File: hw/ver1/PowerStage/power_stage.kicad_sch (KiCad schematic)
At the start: 83 parts, among them J7 Conn_01x02_Socket, Q3 BSS138, Q4 BSS138, Q5 BSS84, Q6 BSS138, SW1 SW_DIP_x03, U2 74HC4051PW, U3 LTC7871, U4 LM1117MP-3.3

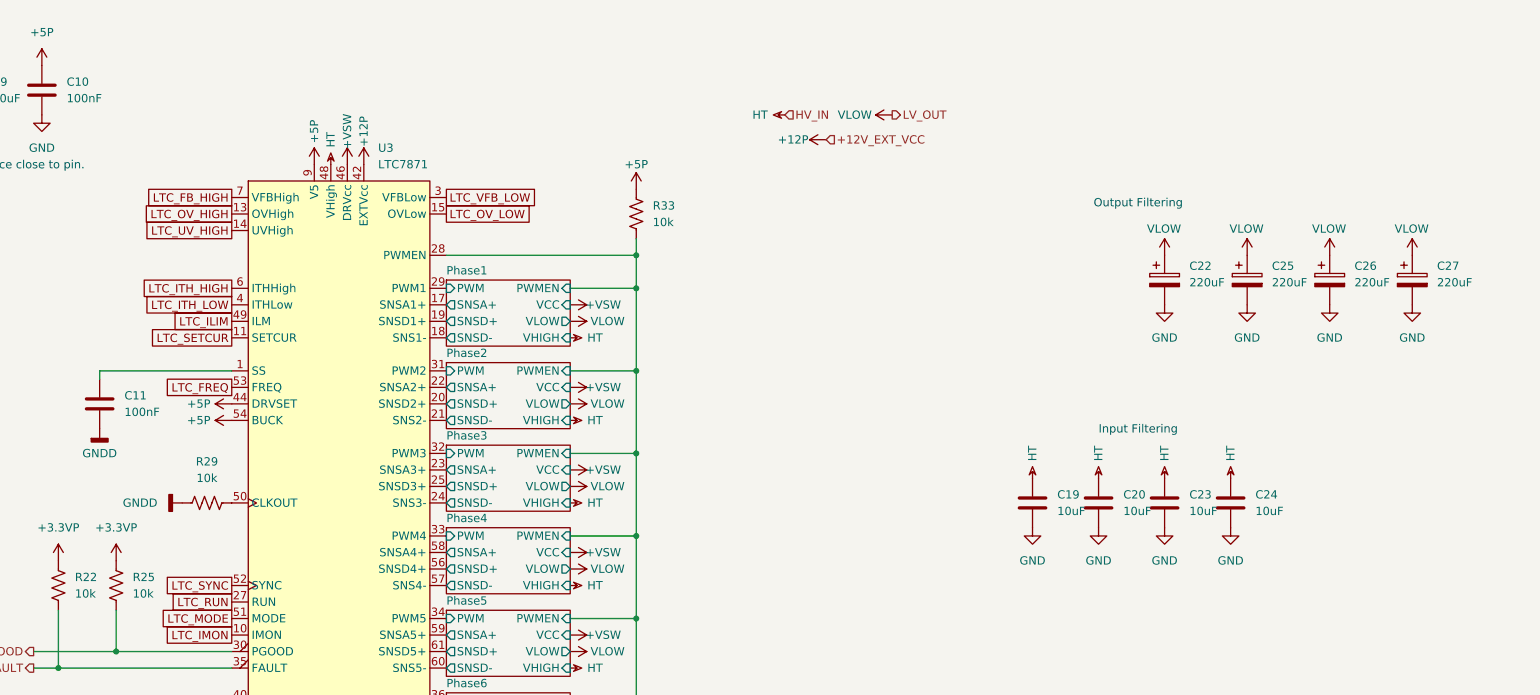
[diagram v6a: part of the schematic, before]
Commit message: Mess with the buck design. Tear out previous approach.
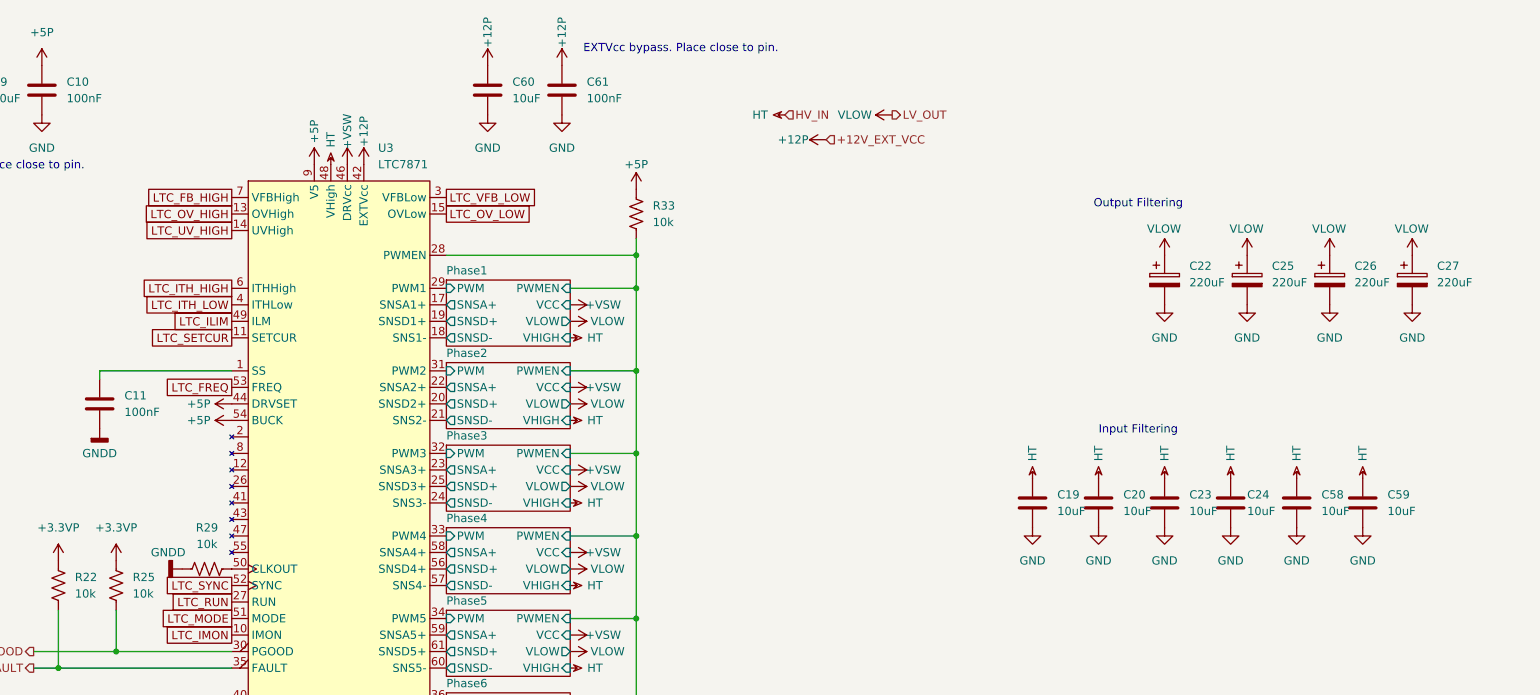
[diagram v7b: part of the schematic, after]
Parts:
- added C58, C59: 10uF, Capacitor_SMD:C_1210_3225Metric_Pad1.33x2.70mm_HandSolder, symbol Device:C
- added C60: 10uF, Capacitor_SMD:C_0603_1608Metric, symbol Device:C
- added C61: 100nF, Capacitor_SMD:C_0603_1608Metric, symbol Device:C
- U2: footprint Package_SO:TSSOP-14_4.4x5mm_P0.65mm -> Package_SO:TSSOP-16_4.4x5mm_P0.65mm
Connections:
- net +12P: now also C60.1, C61.1
- net GND: now also C58.2, C59.2, C60.2, C61.2
- net HT: now also C58.1, C59.1
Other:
- note added: "EXTVcc bypass. Place close to pin."
- moved on the sheet: R29

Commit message: Sync work to laptop
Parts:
- added C62, C63: 220uF, Capacitor_THT:CP_Radial_D10.0mm_P5.00mm, symbol Device:C_Polarized
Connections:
- net GND: now also C62.2, C63.2
- net VLOW: now also C62.1, C63.1
